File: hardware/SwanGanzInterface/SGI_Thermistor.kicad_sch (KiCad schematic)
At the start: 0 parts

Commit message: Added INA122 and OPA2350 in Part Libs, Implimented INA122 in Thermistor Circuit
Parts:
- added C5: 0.1u, Capacitor_SMD:C_0603_1608Metric, symbol Device:C
- added R2: R, symbol Device:R
- added U1: INA122D, Package_SO:SOIC-8_5.3x5.3mm_P1.27mm, symbol SGI_SymbolLib:INA122D
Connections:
- new net: R2.1, U1.1 (RG+)
- new net: R2.2, U1.8 (RG-)
- new net +3V3A: C5.2, U1.7 (+VS)
- new net AGND: C5.1, U1.4 (-VS), U1.5 (REF)

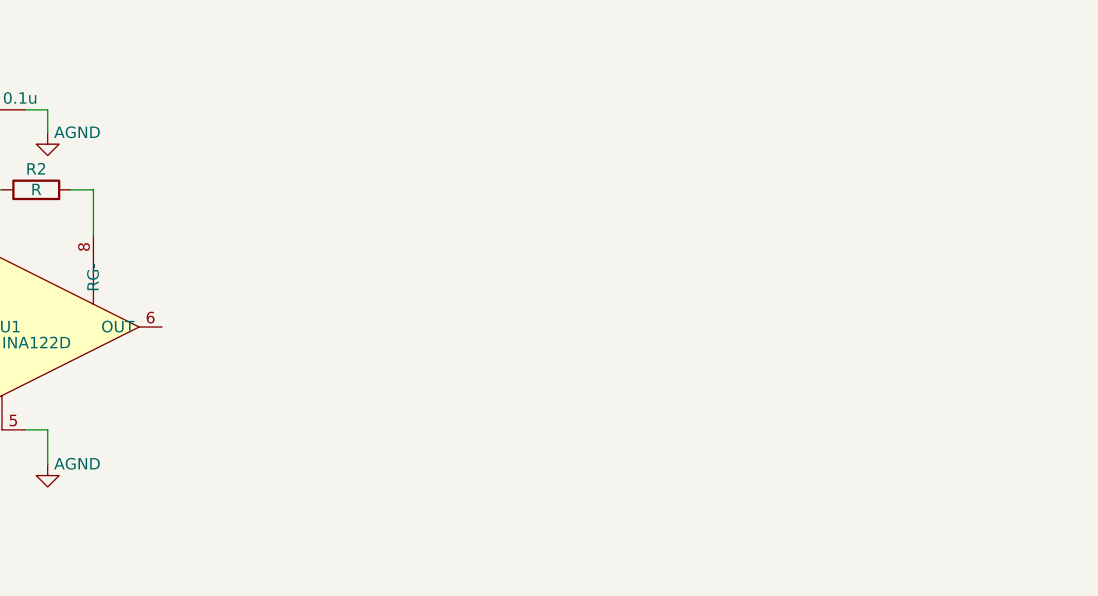
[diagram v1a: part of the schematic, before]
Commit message: Developed amplifier circuits
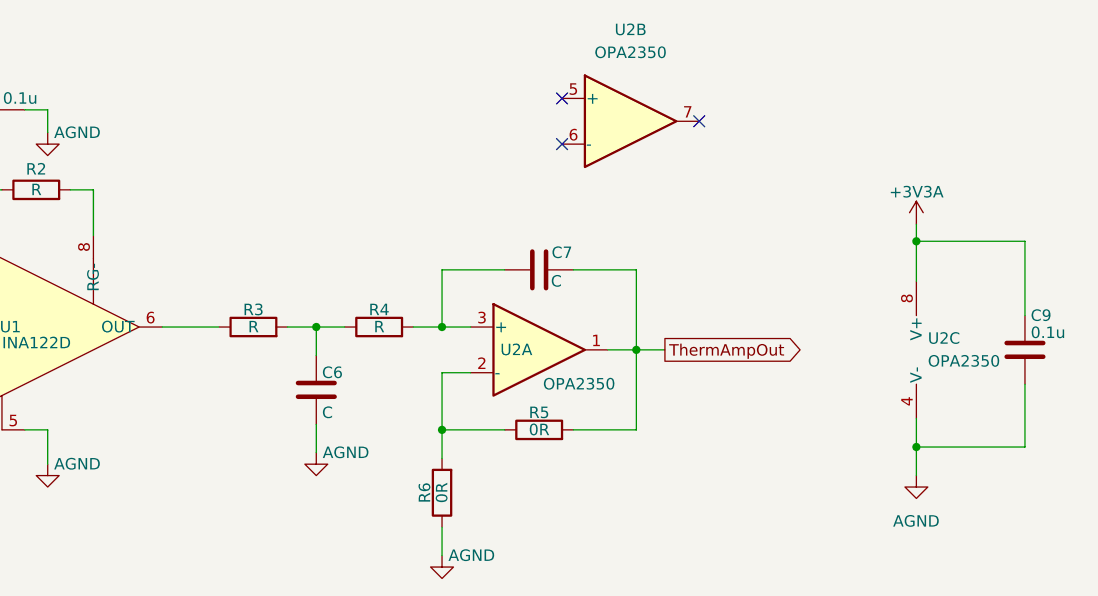
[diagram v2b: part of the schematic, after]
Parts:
- added C6, C7: C, symbol Device:C
- added C9: 0.1u, symbol Device:C
- added R3, R4: R, symbol Device:R
- added R5, R6: 0R, symbol Device:R
- added U2: OPA2350, Package_DIP:DIP-8_W7.62mm, symbol SGI_SymbolLib:OPA2350PA
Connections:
- net +3V3A: now also C9.1, U2.8 (V+)
- net AGND: now also C6.2, C9.2, R6.1, U2.4 (V-)
- net at U1.6 (OUT): now also R3.1
- new net: R5.1, R6.2, U2.2 (-)
- new net: C7.1, R4.2, U2.3 (+)
- new net: C6.1, R3.2, R4.1
- new net ThermAmpOut: C7.2, R5.2, U2.1
- no-connect marks 0 -> 3

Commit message: Filter Parameters
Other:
- note added: "25 Hz Cutoff"
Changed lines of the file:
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@@
 	(generator "eeschema")
 	(generator_version "9.0")
-	(paper "A3")
+	(paper "A4")
 	(title_block
 		(title "Swan Ganz Interface")
-		(date "2025-12-20")
+		(date "2026-01-12")
 		(rev "Rev 1.0")
 		(company "Univerisity of Texas at Austin")
@@
 		(comment 3 "Faculty Mentor - Dr. Valvano")
 	)
+	(text "25 Hz Cutoff\n"
+		(exclude_from_sim no)
+		(at 83.185 85.725 0)
+		(effects
+			(font
+				(size 1.27 1.27)
+			)
+		)
+	)
 	(junction

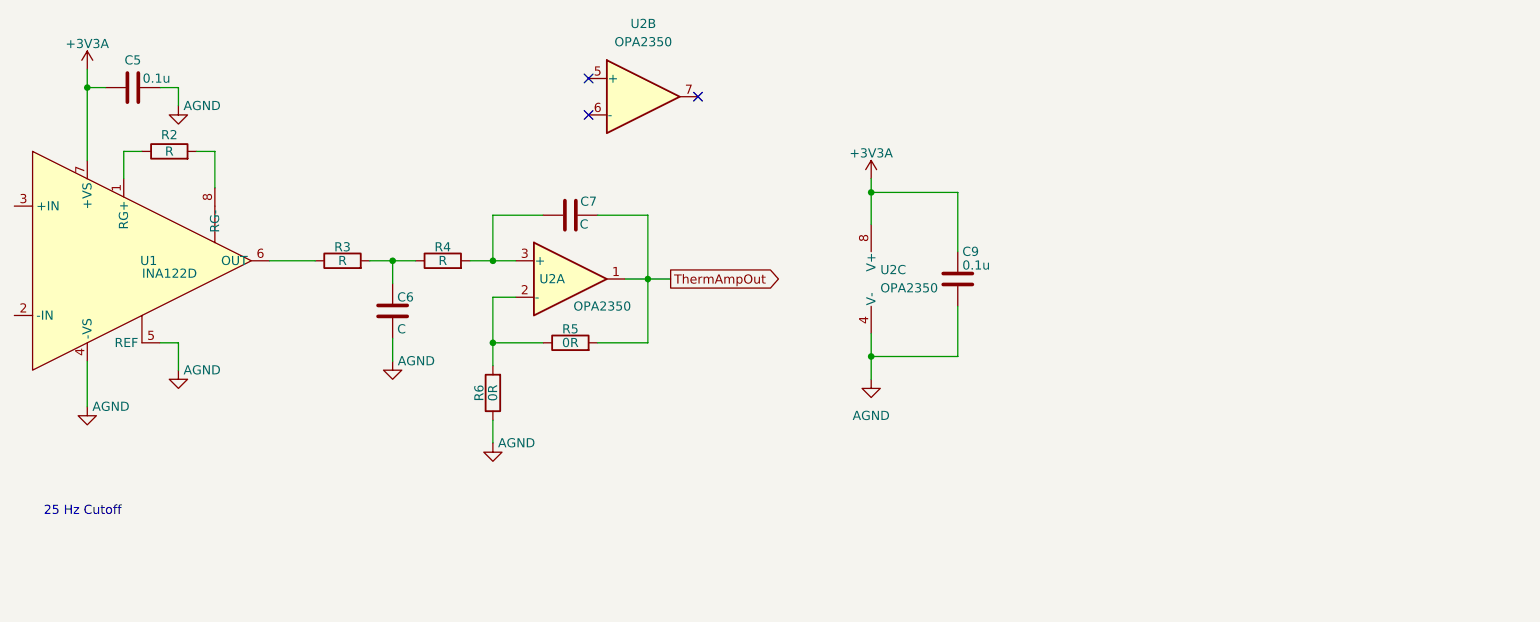
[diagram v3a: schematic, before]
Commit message: Started msp0 symbol
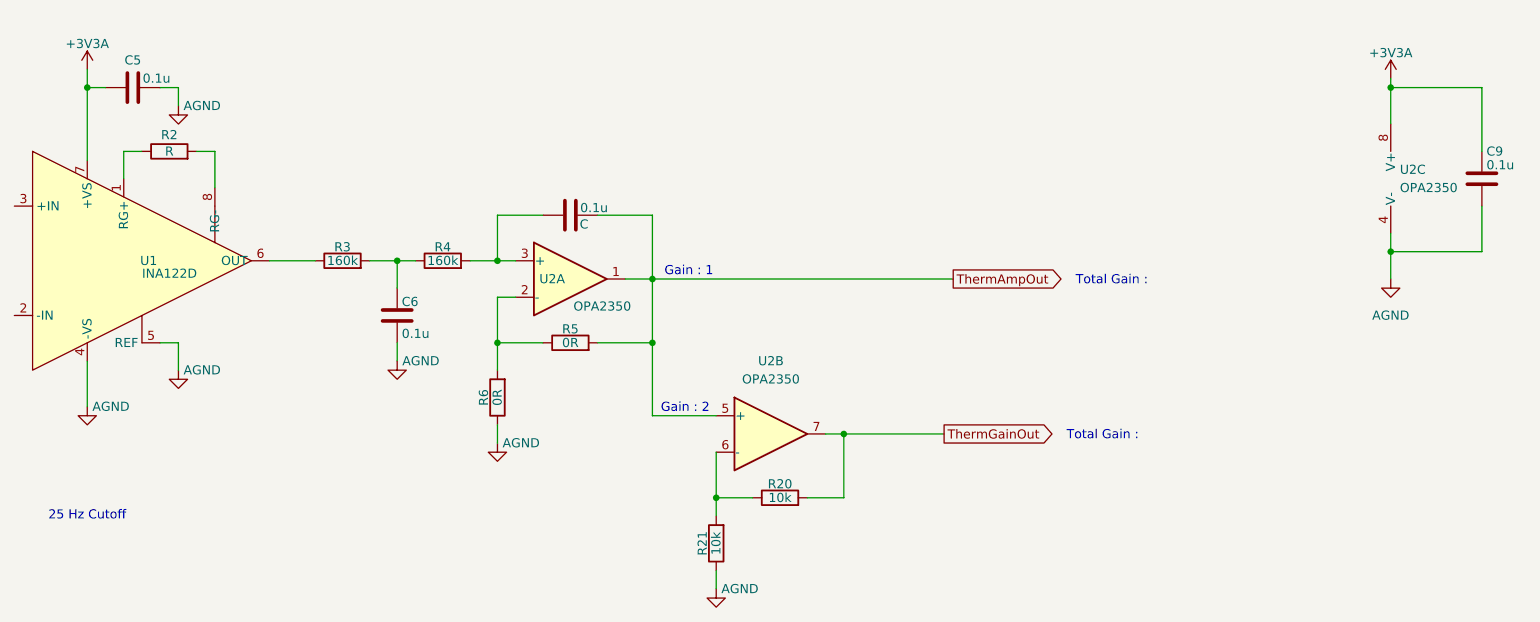
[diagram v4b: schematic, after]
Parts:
- added R20, R21: 10k, symbol Device:R
- C6: value C -> 0.1u
- R3, R4: value R -> 160k
- renumbered C7 to 0.1u
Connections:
- net AGND: now also R21.1
- net ThermAmpOut: now also U2.5 (+)
- net at U2.6 (-): now also R20.1, R21.2
- net ThermGainOut: now reaches U2.7
- net ThermGainOut: now also R20.2
- no-connect marks 3 -> 0
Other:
- note added: "Gain : 1"
- note added: "Gain : 2"
- note added: "Total Gain :"
- moved on the sheet: C6, C9, R6, U2B, U2C
